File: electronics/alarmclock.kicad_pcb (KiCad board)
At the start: 2 copper layers, 15 parts, among them J1 SWD, J4 Conn_01x08, J5 Conn_01x08, SW1 Reset, U1 STM32F030C6T6

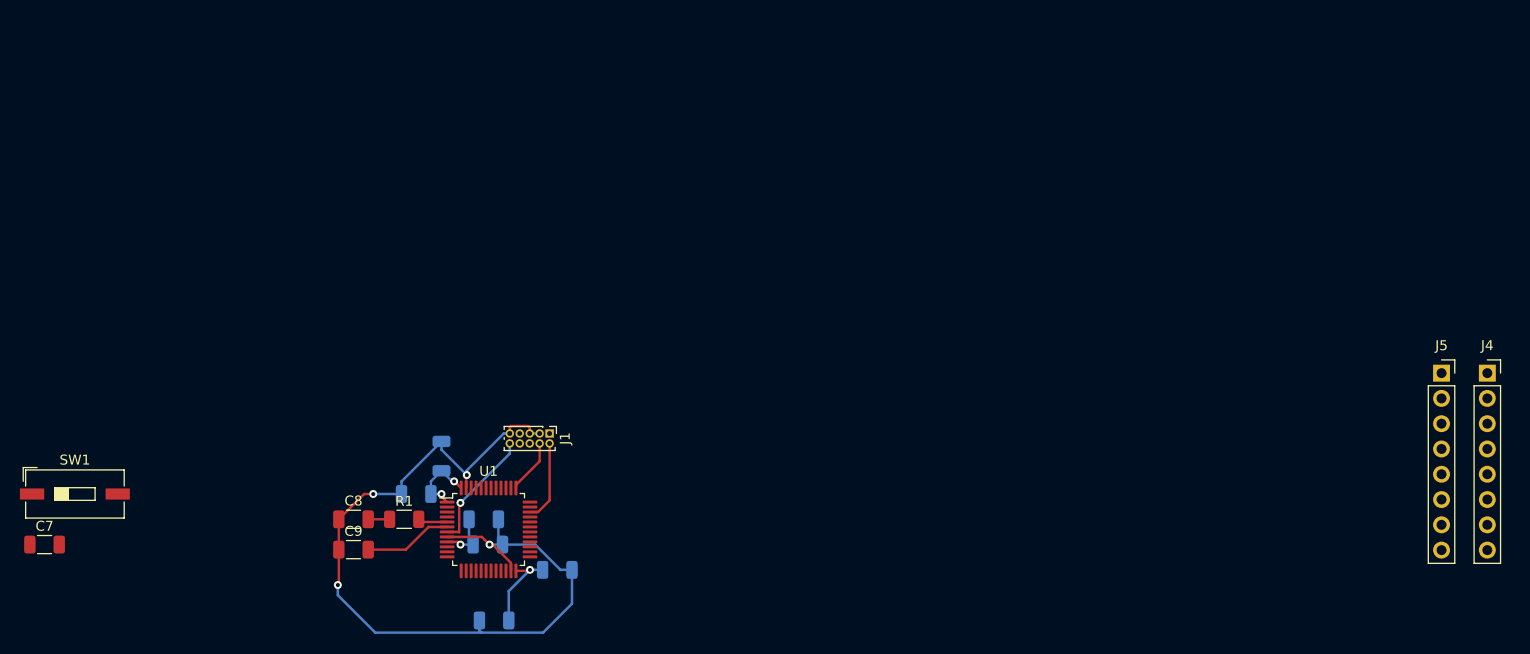
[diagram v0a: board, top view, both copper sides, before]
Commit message: refined pinout, changed solder pad sizes
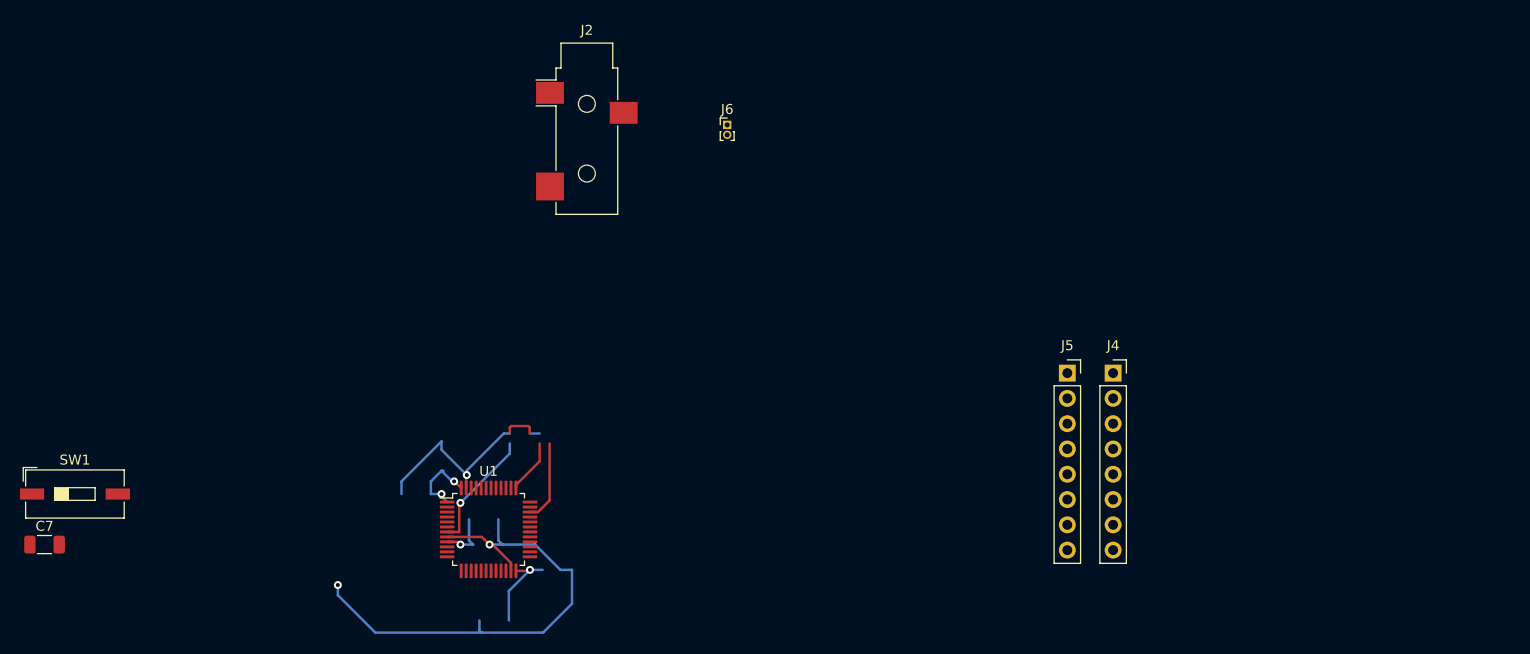
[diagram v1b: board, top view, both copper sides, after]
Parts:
- removed C1: 4.7uF, Capacitor_SMD:C_1206_3216Metric
- removed C2, C3, C4: 100nF, Capacitor_SMD:C_1206_3216Metric
- removed C5: 1uF, Capacitor_SMD:C_1206_3216Metric
- removed C6: 10nF, Capacitor_SMD:C_1206_3216Metric
- removed C8, C9: 12pF, Capacitor_SMD:C_1206_3216Metric
- removed J1: SWD, Connector_PinHeader_1.00mm:PinHeader_2x05_P1.00mm_Vertical
- removed R1: 47R, Resistor_SMD:R_1206_3216Metric
- added J2: AudioJack2, Connector_Audio:Jack_3.5mm_CUI_SJ-3523-SMT_Horizontal, F.Cu at (186.1, 85.2)
- added J6: Barrel_Jack, Connector_PinHeader_1.00mm:PinHeader_1x02_P1.00mm_Vertical, F.Cu at (200.2, 84.8)
- moved J5 37.6 mm to (234.3, 109.8)
- moved J4 37.6 mm to (238.9, 109.8)
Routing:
- net GND: track 89.7 -> 75.8 mm, vias 4 -> 3
- net OSC_OUT: track 8.87 -> 0.00 mm
- net OSC_IN: track 2.96 -> 0.00 mm
- net Net-(C8-Pad2): track 2.16 -> 0.00 mm

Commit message: forgot to save
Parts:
- removed J2: AudioJack2, Connector_Audio:Jack_3.5mm_CUI_SJ-3523-SMT_Horizontal
- added C1: 4.7uF, Capacitor_SMD:C_1206_3216Metric, F.Cu at (185.0, 132.6)
- added C2: 100nF, Capacitor_SMD:C_0201_0603Metric_Pad0.64x0.40mm_HandSolder, F.Cu at (171.2, 121.9)
- added C3: 100nF, Capacitor_SMD:C_0201_0603Metric_Pad0.64x0.40mm_HandSolder, F.Cu at (171.7, 120.4)
- added C4: 100nF, Capacitor_SMD:C_0201_0603Metric_Pad0.64x0.40mm_HandSolder, F.Cu at (180.3, 130.6)
- added C5: 1uF, Capacitor_SMD:C_0805_2012Metric_Pad1.18x1.45mm_HandSolder, B.Cu at (175.8, 127.5)
- added C6: 10nF, Capacitor_SMD:C_0603_1608Metric_Pad1.08x0.95mm_HandSolder, B.Cu at (175.8, 126.0)
- added C8: 12pF, Capacitor_SMD:C_0201_0603Metric_Pad0.64x0.40mm_HandSolder, F.Cu at (165.2, 125.0)
- added C9: 12pF, Capacitor_SMD:C_0201_0603Metric_Pad0.64x0.40mm_HandSolder, F.Cu at (165.1, 127.5)
- added J1: SWD, Connector_PinHeader_1.00mm:PinHeader_2x05_P1.00mm_Vertical, F.Cu at (186.4, 114.8)
- added R1: 47R, Resistor_SMD:R_0201_0603Metric_Pad0.64x0.40mm_HandSolder, F.Cu at (168.2, 125.0)
- C7: footprint Capacitor_SMD:C_1206_3216Metric -> Capacitor_SMD:C_0603_1608Metric_Pad1.08x0.95mm_HandSolder
- moved C7 147.5 mm to (274.0, 88.4)
- moved SW1 141.4 mm to (273.2, 94.2)
- moved J6 44.9 mm to (168.7, 116.8), turned to 180 degrees
- moved J4 12.6 mm to (226.5, 108.0)
- moved J5 12.6 mm to (221.9, 108.0)
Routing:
- net GND: track 75.8 -> 19.0 mm, vias 3 -> 1
- net NRST: track 12.2 -> 0.00 mm, vias 1 -> 0
- net OSC_OUT: track 0.00 -> 7.45 mm
- net +3V3: track 21.9 -> 28.1 mm, vias 4 -> 2
- net SWCLK: track 5.46 -> 9.14 mm
- net OSC_IN: track 0.00 -> 3.48 mm
- net SWDIO: track 8.18 -> 11.5 mm
- net Net-(C8-Pad2): track 0.00 -> 2.21 mm
